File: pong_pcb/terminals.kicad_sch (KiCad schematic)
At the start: 36 parts, among them J3 Screw_Terminal_01x02, J4 Screw_Terminal_01x03, J5 Screw_Terminal_01x03, J6 Screw_Terminal_01x04, J7 Screw_Terminal_01x04, J8 Screw_Terminal_01x02

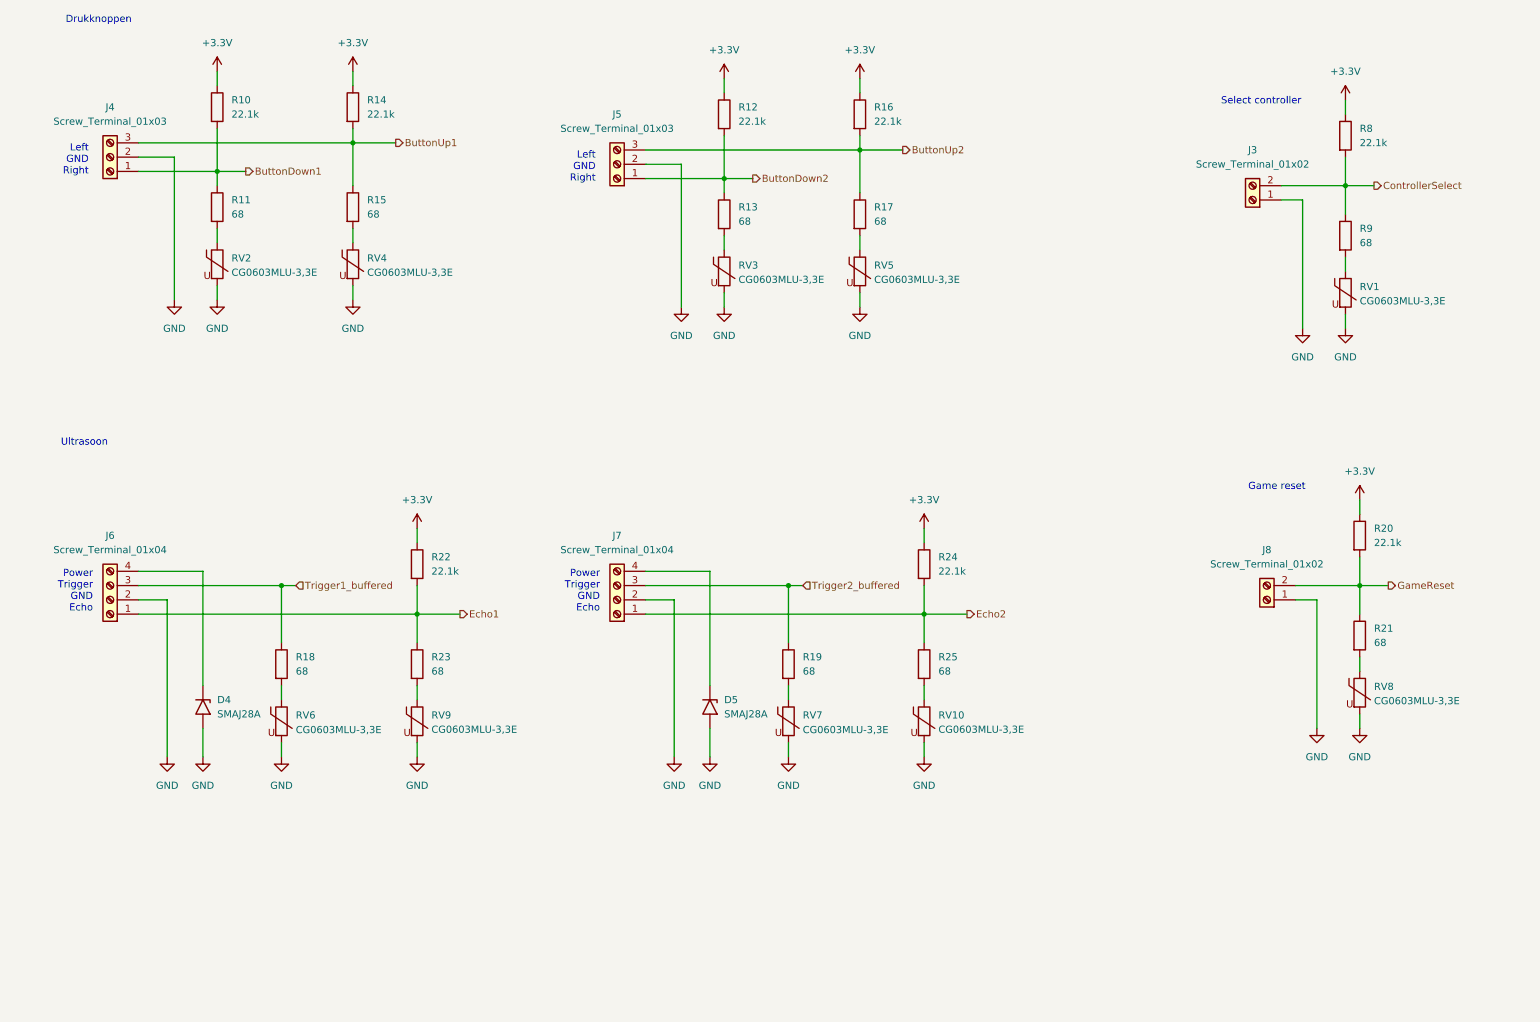
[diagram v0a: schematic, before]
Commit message: Update schema and add packages
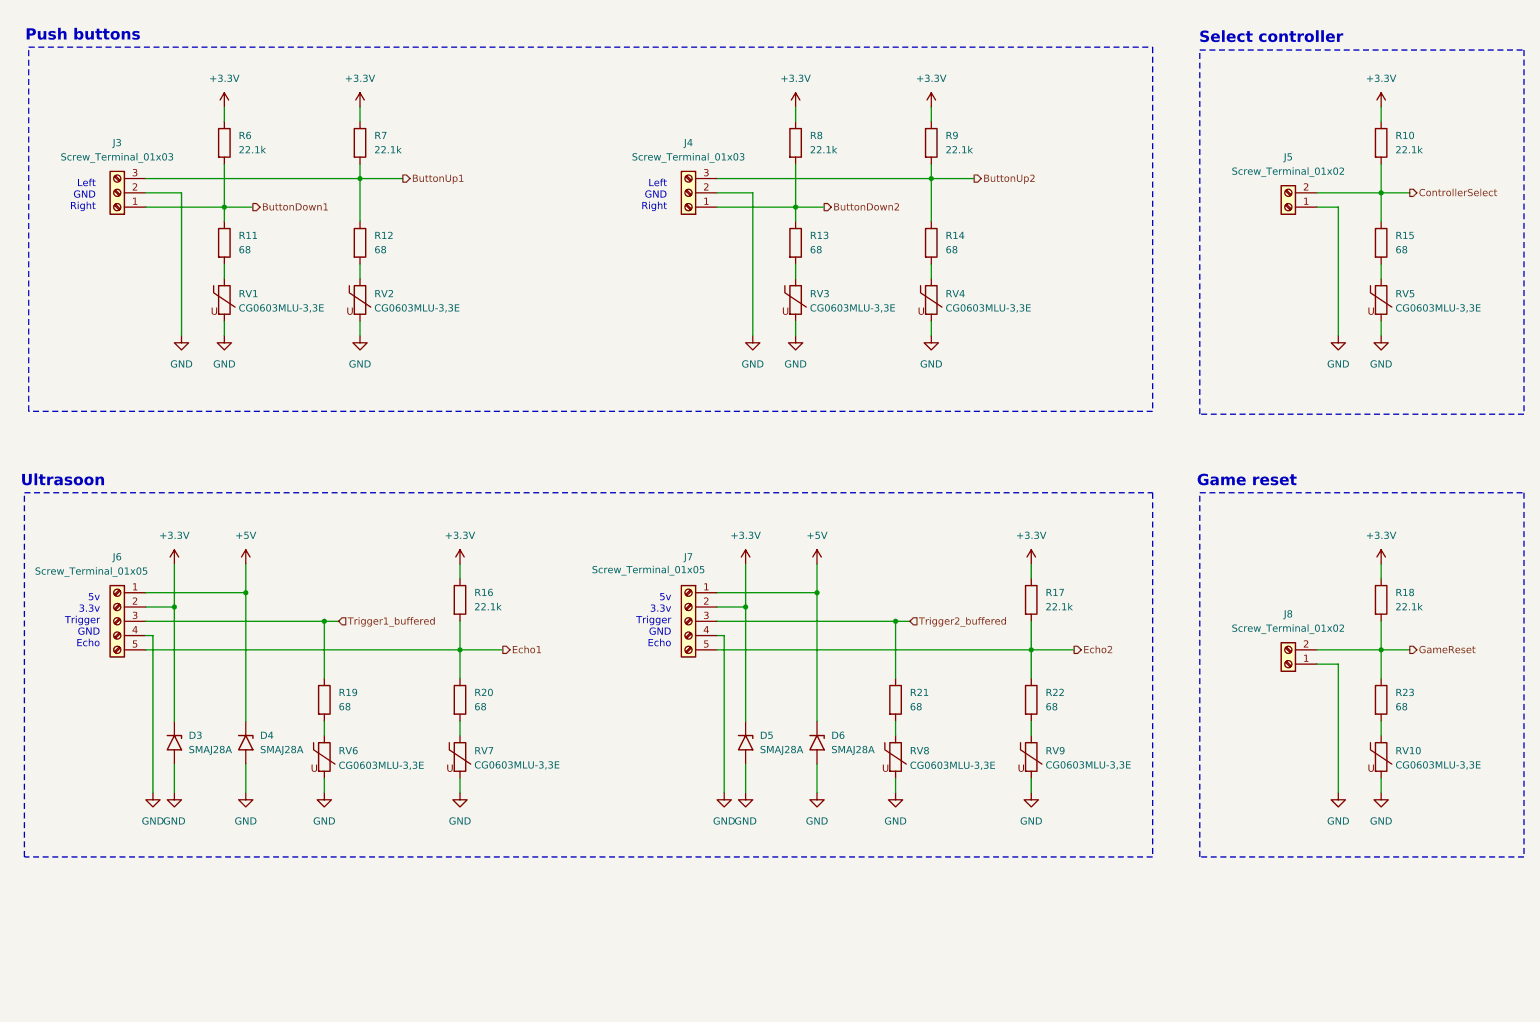
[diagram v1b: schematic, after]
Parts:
- removed J6, J7: Screw_Terminal_01x04, symbol Connector:Screw_Terminal_01x04
- added D3, D6: SMAJ28A, Diode_SMD:D_SMA, symbol Diode:SMAJ28A
- added J6, J7: Screw_Terminal_01x05, TerminalBlock_Phoenix:TerminalBlock_Phoenix_MKDS-1,5-5-5.08_1x05_P5.08mm_Horizontal, symbol Connector:Screw_Terminal_01x05
- J3: renamed from J4; footprint (none) -> TerminalBlock_Phoenix:TerminalBlock_Phoenix_MKDS-1,5-3-5.08_1x03_P5.08mm_Horizontal
- J4: renamed from J5; footprint (none) -> TerminalBlock_Phoenix:TerminalBlock_Phoenix_MKDS-1,5-3-5.08_1x03_P5.08mm_Horizontal
- J5: renamed from J3; footprint (none) -> TerminalBlock_Phoenix:TerminalBlock_Phoenix_MKDS-1,5-2-5.08_1x02_P5.08mm_Horizontal
- J8: footprint (none) -> TerminalBlock_Phoenix:TerminalBlock_Phoenix_MKDS-1,5-2-5.08_1x02_P5.08mm_Horizontal
- R10: renamed from R8; footprint (none) -> Resistor_SMD:R_0603_1608Metric
- R11, R13: footprint (none) -> Resistor_SMD:R_0603_1608Metric
- R12: renamed from R15; footprint (none) -> Resistor_SMD:R_0603_1608Metric
- R14: renamed from R17; footprint (none) -> Resistor_SMD:R_0603_1608Metric
- R15: renamed from R9; footprint (none) -> Resistor_SMD:R_0603_1608Metric
- R16: renamed from R22; footprint (none) -> Resistor_SMD:R_0603_1608Metric
- R17: renamed from R24; footprint (none) -> Resistor_SMD:R_0603_1608Metric
- R18: renamed from R20; footprint (none) -> Resistor_SMD:R_0603_1608Metric
- R19: renamed from R18; footprint (none) -> Resistor_SMD:R_0603_1608Metric
- R20: renamed from R23; footprint (none) -> Resistor_SMD:R_0603_1608Metric
- R21: renamed from R19; footprint (none) -> Resistor_SMD:R_0603_1608Metric
- R22: renamed from R25; footprint (none) -> Resistor_SMD:R_0603_1608Metric
- R23: renamed from R21; footprint (none) -> Resistor_SMD:R_0603_1608Metric
- R6: renamed from R10; footprint (none) -> Resistor_SMD:R_0603_1608Metric
- R7: renamed from R14; footprint (none) -> Resistor_SMD:R_0603_1608Metric
- R8: renamed from R12; footprint (none) -> Resistor_SMD:R_0603_1608Metric
- R9: renamed from R16; footprint (none) -> Resistor_SMD:R_0603_1608Metric
- renumbered RV2 to RV1, RV8 to RV10, RV4 to RV2, RV5 to RV4, RV1 to RV5, RV9 to RV7, RV7 to RV8, RV10 to RV9
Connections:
- net +3.3V: now also D5.1 (A1), D3.1 (A1), J6.2 (Pin_2), J7.2 (Pin_2)
- net Echo1: now also J6.5 (Pin_5)
- net Echo2: now also J7.5 (Pin_5)
- net GND: now also D3.2 (A2), D6.2 (A2), J6.4 (Pin_4), J7.4 (Pin_4)
- net Trigger1_buffered: now also J6.3 (Pin_3)
- net Trigger2_buffered: now also J7.3 (Pin_3)
- net +5V: now reaches D4.1 (A1)
- net +5V: now also D6.1 (A1), J6.1 (Pin_1), J7.1 (Pin_1)
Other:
- note added: "5v 3.3v Trigger GND Echo"
- note added: "Push buttons"
- note removed: "Drukknoppen"
- note removed: "Power Trigger GND Echo"
- company: (none) -> Fontys
- title: (none) -> Terminals
- moved on the sheet: D4, J3, J4, J5, J8, R10, R11, R12, R13, R14, R15, R16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

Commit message: Add HDMI layout
And others
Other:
- note added: "Left player"
- note added: "Right Player"
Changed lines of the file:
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@@
+		)
+	)
+	(text "Left player"
+		(exclude_from_sim no)
+		(at 31.496 22.098 0)
+		(effects
+			(font
+				(size 1.27 1.27)
+			)
+		)
+	)
+	(text "Right Player"
+		(exclude_from_sim no)
+		(at 133.858 21.844 0)
+		(effects
+			(font
+				(size 1.27 1.27)
+			)
 		)
 	)
@@
 			)
 		)
+	)
+	(text "Right Player"
+		(exclude_from_sim no)
+		(at 133.35 102.108 0)
+		(effects
+			(font
+				(size 1.27 1.27)
+			)
+		)
+	)
+	(text "Left player"
+		(exclude_from_sim no)
+		(at 31.242 101.346 0)
+		(effects
+			(font
+				(size 1.27 1.27)
+			)
+		)

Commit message: Update schema and route PCB
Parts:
- added C22, C23, C24, C25: 100n 10v, Capacitor_SMD:C_0603_1608Metric, symbol Device:C
- added C26: 47u 10v, Capacitor_SMD:C_1206_3216Metric_Pad1.33x1.80mm_HandSolder, symbol Device:C
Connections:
- net +3.3V: now also C22.1, C24.1, C26.1
- net +5V: now also C23.1, C25.1
- net GND: now also C22.2, C23.2, C24.2, C25.2, C26.2

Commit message: Other connectors
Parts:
- J3, J4: footprint TerminalBlock_Phoenix:TerminalBlock_Phoenix_MKDS-1,5-3-5.08_1x03_P5.08mm_Horizontal -> Connector_Phoenix_MSTB:PhoenixContact_MSTBA_2,5_3-G-5,08_1x03_P5.08mm_Horizontal
- J5, J8: footprint TerminalBlock_Phoenix:TerminalBlock_Phoenix_MKDS-1,5-2-5.08_1x02_P5.08mm_Horizontal -> Connector_Phoenix_MSTB:PhoenixContact_MSTBA_2,5_2-G-5,08_1x02_P5.08mm_Horizontal
- J6, J7: footprint TerminalBlock_Phoenix:TerminalBlock_Phoenix_MKDS-1,5-5-5.08_1x05_P5.08mm_Horizontal -> Connector_Phoenix_MSTB:PhoenixContact_MSTBA_2,5_5-G-5,08_1x05_P5.08mm_Horizontal
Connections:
- net +3.3V: now also J6.4 (Pin_4), J7.4 (Pin_4); no longer J6.2 (Pin_2), J7.2 (Pin_2)
- net +5V: now also J6.5 (Pin_5), J7.5 (Pin_5); no longer J6.1 (Pin_1), J7.1 (Pin_1)
- net ButtonDown1: now also J3.3 (Pin_3); no longer J3.1 (Pin_1)
- net ButtonDown2: now also J4.3 (Pin_3); no longer J4.1 (Pin_1)
- net ButtonUp1: now also J3.1 (Pin_1); no longer J3.3 (Pin_3)
- net ButtonUp2: now also J4.1 (Pin_1); no longer J4.3 (Pin_3)
- net ControllerSelect: now also J5.1 (Pin_1); no longer J5.2 (Pin_2)
- net Echo1: now also J6.1 (Pin_1); no longer J6.5 (Pin_5)
- net Echo2: now also J7.1 (Pin_1); no longer J7.5 (Pin_5)
- net GND: now also J5.2 (Pin_2), J6.2 (Pin_2), J7.2 (Pin_2), J8.2 (Pin_2); no longer J5.1 (Pin_1), J6.4 (Pin_4), J7.4 (Pin_4), J8.1 (Pin_1)
- net GameReset: now also J8.1 (Pin_1); no longer J8.2 (Pin_2)
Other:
- moved on the sheet: J3, J4, J5, J6, J7, J8
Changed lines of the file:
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@@
 	(symbol
 		(lib_id "Connector:Screw_Terminal_01x02")
-		(at 240.03 46.99 180)
+		(at 240.03 44.45 0)
+		(mirror y)
 		(unit 1)
 		(exclude_from_sim no)
@@
 		(on_board yes)
 		(dnp no)
-		(fields_autoplaced yes)
 		(property "Reference" "J5"
-			(at 240.03 38.1 0)
+			(at 239.776 38.354 0)
 			(effects
 				(font
@@
 			)
 		)
-		(property "Footprint" "TerminalBlock_Phoenix:TerminalBlock_Phoenix_MKDS-1,5-2-5.08_1x02_P5.08mm_Horizontal"
-			(at 240.03 46.99 0)
+		(property "Footprint" "Connector_Phoenix_MSTB:PhoenixContact_MSTBA_2,5_2-G-5,08_1x02_P5.08mm_Horizontal"
+			(at 240.03 44.45 0)
 			(effects
 				(font
@@
 		)
 		(property "Datasheet" "~"
-			(at 240.03 46.99 0)
+			(at 240.03 44.45 0)
 			(effects
 				(font
@@
 		)
 		(property "Description" "Generic screw terminal, single row, 01x02, script generated (kicad-library-utils/schlib/autogen/connector/)"
-			(at 240.03 46.99 0)
+			(at 240.03 44.45 0)
 			(effects
 				(font
@@
 	(symbol
 		(lib_id "Connector:Screw_Terminal_01x03")
-		(at 31.75 44.45 180)
+		(at 31.75 44.45 0)
+		(mirror y)
 		(unit 1)
 		(exclude_from_sim no)
@@
 		(dnp no)
 		(property "Reference" "J3"
-			(at 31.75 35.56 0)
+			(at 31.75 36.576 0)
 			(effects
 				(font
@@
 		)
 		(property "Value" "Screw_Terminal_01x03"
-			(at 31.75 38.1 0)
+			(at 31.242 38.862 0)
 			(effects
 				(font
@@
 			)
 		)
-		(property "Footprint" "TerminalBlock_Phoenix:TerminalBlock_Phoenix_MKDS-1,5-3-5.08_1x03_P5.08mm_Horizontal"
+		(property "Footprint" "Connector_Phoenix_MSTB:PhoenixContact_MSTBA_2,5_3-G-5,08_1x03_P5.08mm_Horizontal"
 			(at 31.75 44.45 0)
 			(effects
@@
 	(symbol
 		(lib_id "Connector:Screw_Terminal_01x02")
-		(at 240.03 128.27 180)
+		(at 240.03 125.73 0)
+		(mirror y)
 		(unit 1)
 		(exclude_from_sim no)
@@
 		(on_board yes)
 		(dnp no)
-		(fields_autoplaced yes)
 		(property "Reference" "J8"
-			(at 240.03 119.38 0)
+			(at 239.776 119.888 0)
 			(effects
 				(font
@@
 			)
 		)
-		(property "Footprint" "TerminalBlock_Phoenix:TerminalBlock_Phoenix_MKDS-1,5-2-5.08_1x02_P5.08mm_Horizontal"
-			(at 240.03 128.27 0)
+		(property "Footprint" "Connector_Phoenix_MSTB:PhoenixContact_MSTBA_2,5_2-G-5,08_1x02_P5.08mm_Horizontal"
+			(at 240.03 125.73 0)
 			(effects
 				(font
@@
 		)
 		(property "Datasheet" "~"
-			(at 240.03 128.27 0)
+			(at 240.03 125.73 0)
 			(effects
 				(font
@@
 		)
 		(property "Description" "Generic screw terminal, single row, 01x02, script generated (kicad-library-utils/schlib/autogen/connector/)"
-			(at 240.03 128.27 0)
+			(at 240.03 125.73 0)
 			(effects
 				(font
@@
 	(symbol
 		(lib_id "Connector:Screw_Terminal_01x05")
-		(at 31.75 120.65 0)
-		(mirror y)
+		(at 31.75 120.65 180)
 		(unit 1)
 		(exclude_from_sim no)
@@
 		(dnp no)
 		(property "Reference" "J6"
-			(at 31.75 109.22 0)
+			(at 31.75 108.966 0)
 			(effects
 				(font
@@
 		)
 		(property "Value" "Screw_Terminal_01x05"
-			(at 27.178 111.76 0)
+			(at 29.21 111.76 0)
 			(effects
 				(font
@@
 			)
 		)
-		(property "Footprint" "TerminalBlock_Phoenix:TerminalBlock_Phoenix_MKDS-1,5-5-5.08_1x05_P5.08mm_Horizontal"
+		(property "Footprint" "Connector_Phoenix_MSTB:PhoenixContact_MSTBA_2,5_5-G-5,08_1x05_P5.08mm_Horizontal"
 			(at 31.75 120.65 0)
 			(effects
@@
 	(symbol
 		(lib_id "Connector:Screw_Terminal_01x05")
-		(at 133.35 120.65 0)
-		(mirror y)
+		(at 133.35 120.65 180)
 		(unit 1)
 		(exclude_from_sim no)
@@
 		(dnp no)
 		(property "Reference" "J7"
-			(at 133.35 109.22 0)
+			(at 133.604 109.728 0)
 			(effects
 				(font
@@
 		)
 		(property "Value" "Screw_Terminal_01x05"
-			(at 126.238 111.506 0)
+			(at 131.318 111.76 0)
 			(effects
 				(font
@@
 			)
 		)
-		(property "Footprint" "TerminalBlock_Phoenix:TerminalBlock_Phoenix_MKDS-1,5-5-5.08_1x05_P5.08mm_Horizontal"
+		(property "Footprint" "Connector_Phoenix_MSTB:PhoenixContact_MSTBA_2,5_5-G-5,08_1x05_P5.08mm_Horizontal"
 			(at 133.35 120.65 0)
 			(effects
@@
 	(symbol
 		(lib_id "Connector:Screw_Terminal_01x03")
-		(at 133.35 44.45 180)
+		(at 133.35 44.45 0)
+		(mirror y)
 		(unit 1)
 		(exclude_from_sim no)
@@
 			)
 		)
-		(property "Footprint" "TerminalBlock_Phoenix:TerminalBlock_Phoenix_MKDS-1,5-3-5.08_1x03_P5.08mm_Horizontal"
+		(property "Footprint" "Connector_Phoenix_MSTB:PhoenixContact_MSTBA_2,5_3-G-5,08_1x03_P5.08mm_Horizontal"
 			(at 133.35 44.45 0)
 			(effects
